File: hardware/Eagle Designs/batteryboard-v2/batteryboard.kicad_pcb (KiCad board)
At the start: 2 copper layers, 95.9 x 90.2 mm, 43 parts, among them J1 KEYSTONE-1042, J10 Conn_01x02_Female, J11 Conn_01x04_Female, J12 Screw_Terminal_01x01, J2 KEYSTONE-1042, J3 KEYSTONE-1042, J4 KEYSTONE-1042, J5 KEYSTONE-1042, J6 KEYSTONE-1042, J7 Conn_01x02_Female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

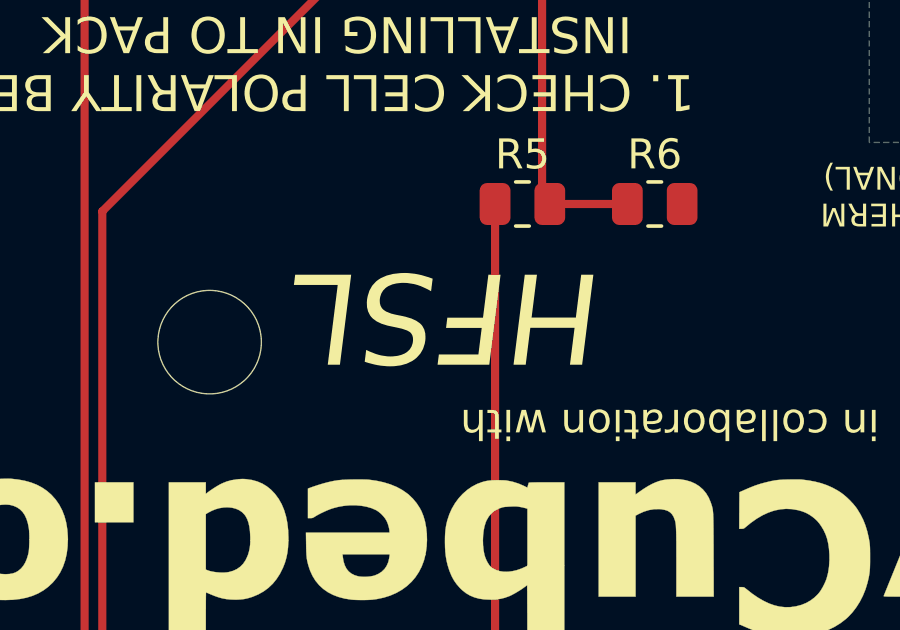
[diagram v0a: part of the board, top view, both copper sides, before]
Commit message: Battery board text changes
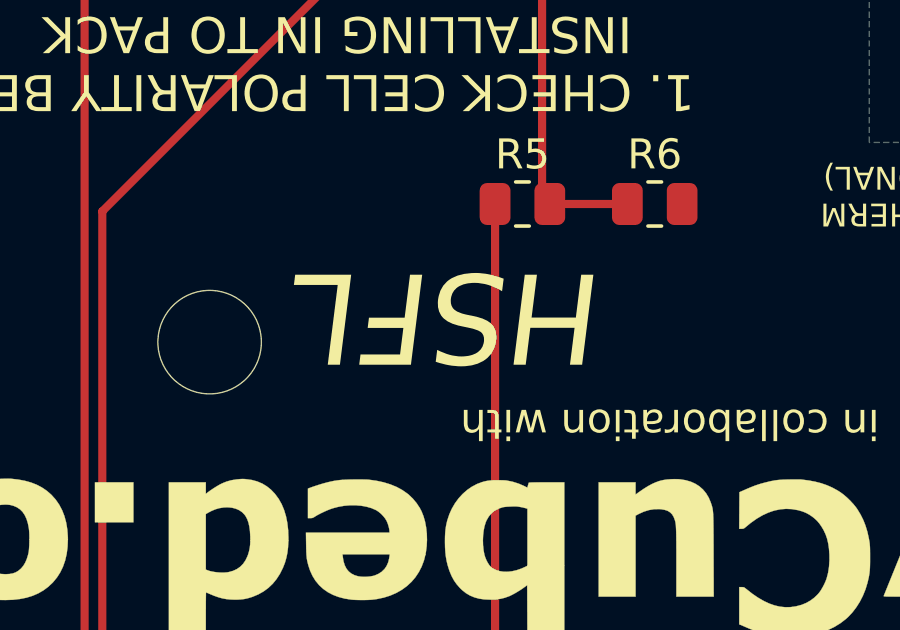
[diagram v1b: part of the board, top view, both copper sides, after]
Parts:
- removed the Ref** at (111.4, 56.4)
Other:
- board text added: "HSFL"
- board text added: "batteryboard.v2"
- board text removed: "HFSL"
